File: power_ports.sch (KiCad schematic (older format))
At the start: 192 parts, among them J0 phoenix_1935161, J1 phoenix_1935161, J10 phoenix_1935161, J11 phoenix_1935161, J12 phoenix_1935161, J13 phoenix_1935161, J14 phoenix_1935161, J15 phoenix_1935161, J16 phoenix_1935161, J17 phoenix_1935161, J18 phoenix_1935161, J19 phoenix_1935161, J2 phoenix_1935161, J20 phoenix_1935161, J21 phoenix_1935161, J22 phoenix_1935161, J23 phoenix_1935161, J24 phoenix_1935161, J25 phoenix_1935161, J26 phoenix_1935161, J27 phoenix_1935161, J28 phoenix_1935161, J29 phoenix_1935161, J3 phoenix_1935161, J30 phoenix_1935161, J31 phoenix_1935161, J32 phoenix_1935161, J33 phoenix_1935161, J34 phoenix_1935161, J35 phoenix_1935161, J36 phoenix_1935161, J37 phoenix_1935161, J38 phoenix_1935161, J39 phoenix_1935161, J4 phoenix_1935161, J40 phoenix_1935161, J41 phoenix_1935161, J42 phoenix_1935161, J43 phoenix_1935161, J44 phoenix_1935161, J45 phoenix_1935161, J46 phoenix_1935161, J47 phoenix_1935161, J48 phoenix_1935161, J49 phoenix_1935161, J5 phoenix_1935161, J50 phoenix_1935161, J51 phoenix_1935161, J52 phoenix_1935161, J53 phoenix_1935161, J54 phoenix_1935161, J55 phoenix_1935161, J56 phoenix_1935161, J57 phoenix_1935161, J58 phoenix_1935161, J59 phoenix_1935161, J6 phoenix_1935161, J60 phoenix_1935161, J61 phoenix_1935161, J62 phoenix_1935161, J63 phoenix_1935161, J7 phoenix_1935161, J8 phoenix_1935161, J9 phoenix_1935161, Q0 Q_NMOS_GSD, Q1 Q_NMOS_GSD, Q10 Q_NMOS_GSD, Q11 Q_NMOS_GSD, Q12 Q_NMOS_GSD, Q13 Q_NMOS_GSD, Q14 Q_NMOS_GSD, Q15 Q_NMOS_GSD, Q16 Q_NMOS_GSD, Q17 Q_NMOS_GSD, Q18 Q_NMOS_GSD, Q19 Q_NMOS_GSD, Q2 Q_NMOS_GSD, Q20 Q_NMOS_GSD, Q21 Q_NMOS_GSD, Q22 Q_NMOS_GSD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

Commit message: 64 port hat
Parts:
- Q0, Q1, Q10, Q11, Q12, Q13, Q14, Q15, Q16, Q17, Q18, Q19, Q2, Q20, Q21, Q22, Q23, Q24, Q25, Q26, Q27, Q28, Q29, Q3, Q30, Q31, Q32, Q33, Q34, Q35, Q36, Q37, Q38, Q39, Q4, Q40, Q41, Q42, Q43, Q44, Q45, Q46, Q47, Q48, Q49, Q5, Q50, Q51, Q52, Q53, Q54, Q55, Q56, Q57, Q58, Q59, Q6, Q60, Q61, Q62, Q63, Q7, Q8, Q9: DPN DMG2302UK-7DICT-ND -> IRLML6244TRPBFCT-ND; MPN DMG2302UK-7 -> (none); PN DMG2302UK-7 -> IRLML6244TRPBF; URL https://www.digikey.com/product-detail/en/diodes-incorporat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 -> https://www.digikey.com/product-detail/en/infineon-technolo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

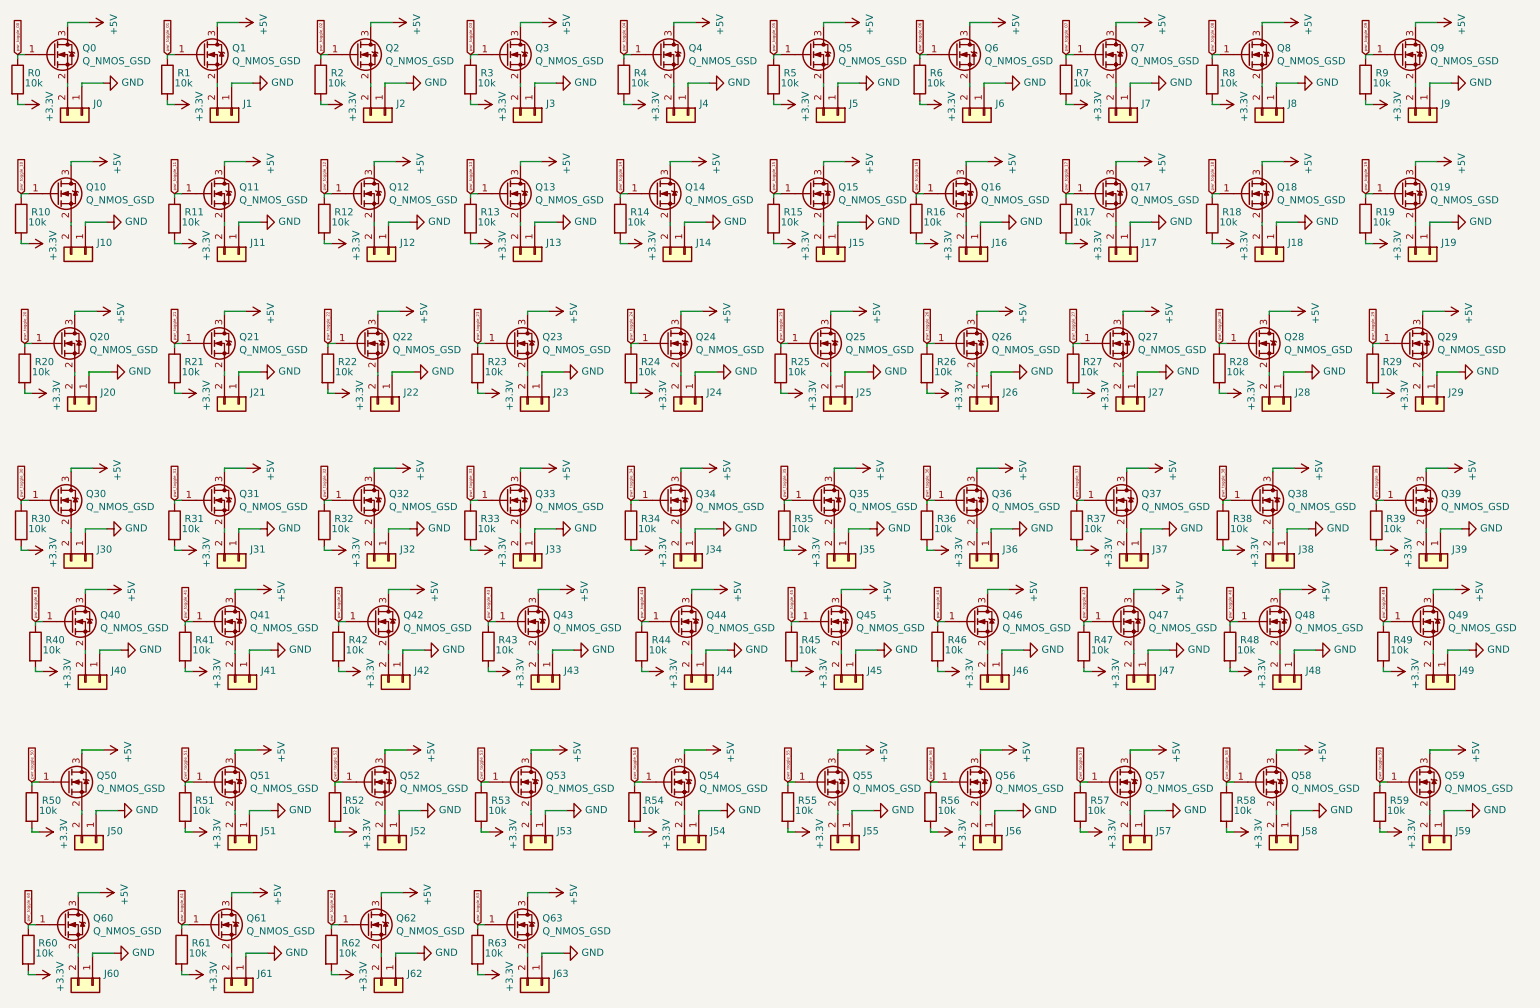
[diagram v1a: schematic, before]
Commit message: PCB routed for 48 ports
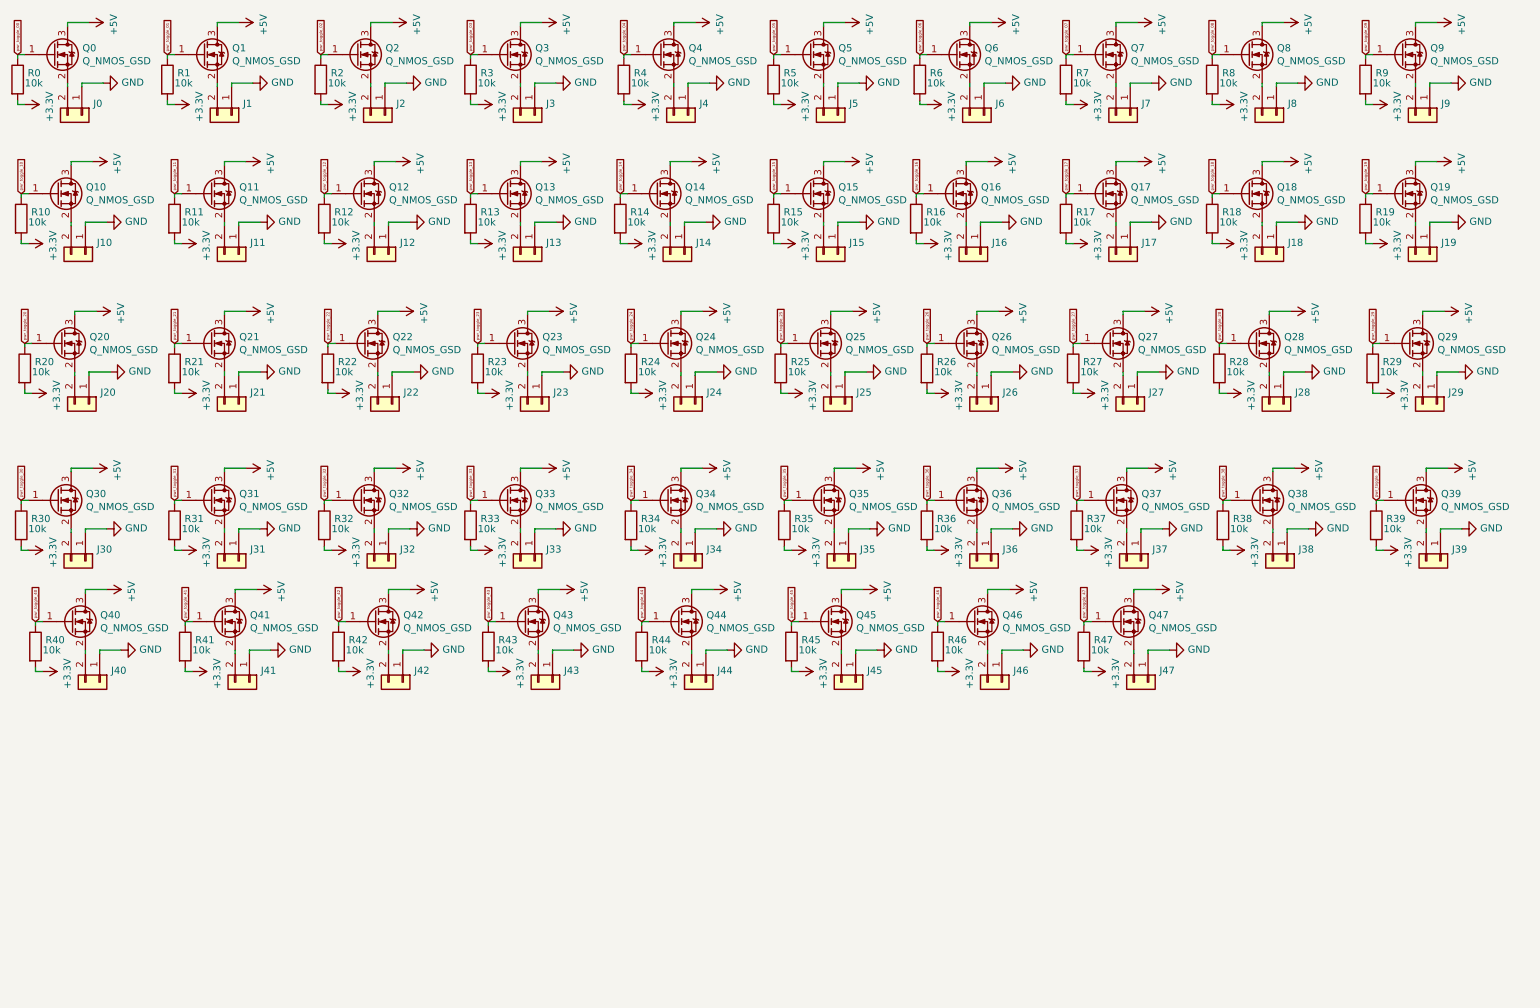
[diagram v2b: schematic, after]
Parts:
- removed J48, J49, J50, J51, J52, J53, J54, J55, J56, J57, J58, J59, J60, J61, J62, J63: phoenix_1935161, lib:PHOENIX_1935161, symbol atv_cluster_hat:phoenix_1935161
- removed Q48, Q49, Q50, Q51, Q52, Q53, Q54, Q55, Q56, Q57, Q58, Q59, Q60, Q61, Q62, Q63: Q_NMOS_GSD, Package_TO_SOT_SMD:SOT-23_Handsoldering, symbol Device:Q_NMOS_GSD
- removed R48, R49, R50, R51, R52, R53, R54, R55, R56, R57, R58, R59, R60, R61, R62, R63: 10k, Resistor_SMD:R_1206_3216Metric_Pad1.42x1.75mm_HandSolder, symbol Device:R
